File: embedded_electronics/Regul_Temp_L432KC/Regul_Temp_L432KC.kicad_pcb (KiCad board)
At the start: 2 copper layers, 88.9 x 70.1 mm, 31 parts, among them J1 TRIM_CONSIGNE, J11 Digilent Motor, J12 2.54 motor, J2 Temp_In, J3 POWER_IN_5V, J4 SW_MODE, J5 OUT_to_BNC, J6 Consigne, J7 Erreur, J8 OLED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

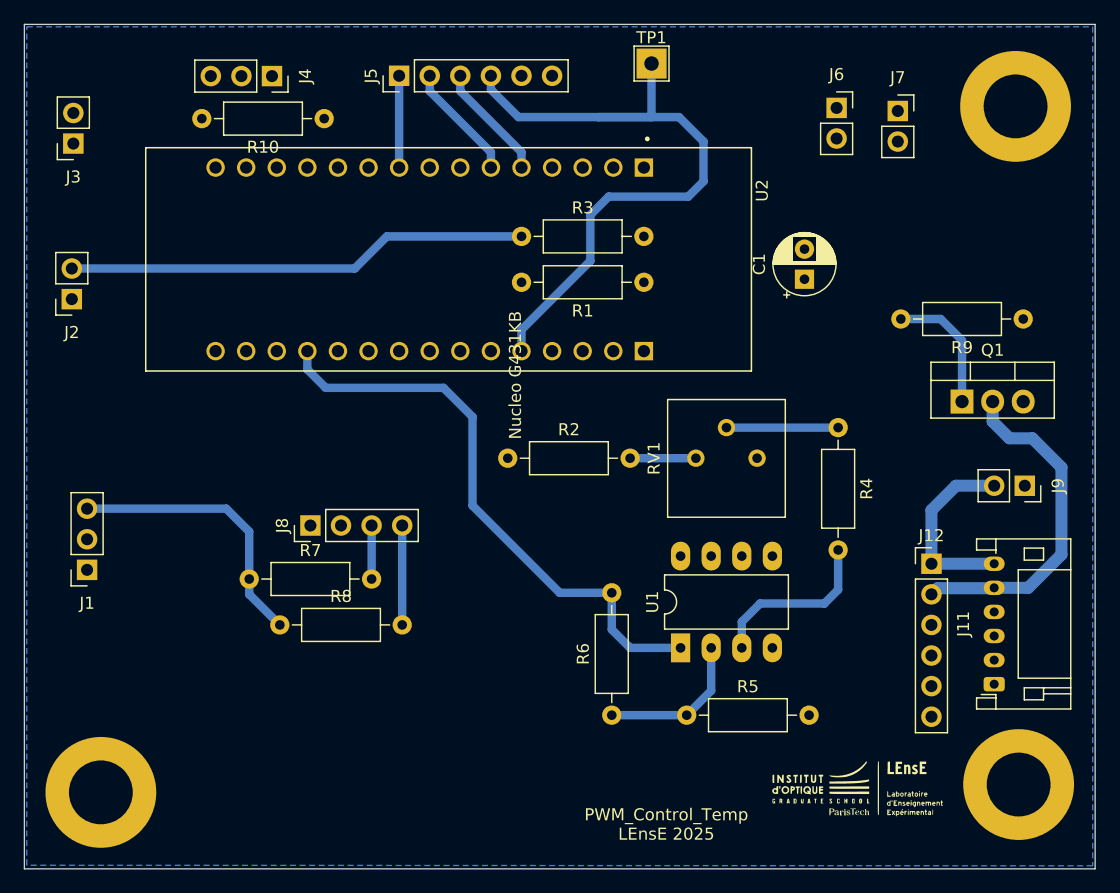
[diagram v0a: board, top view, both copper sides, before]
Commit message: Update PCB of Regulation platform
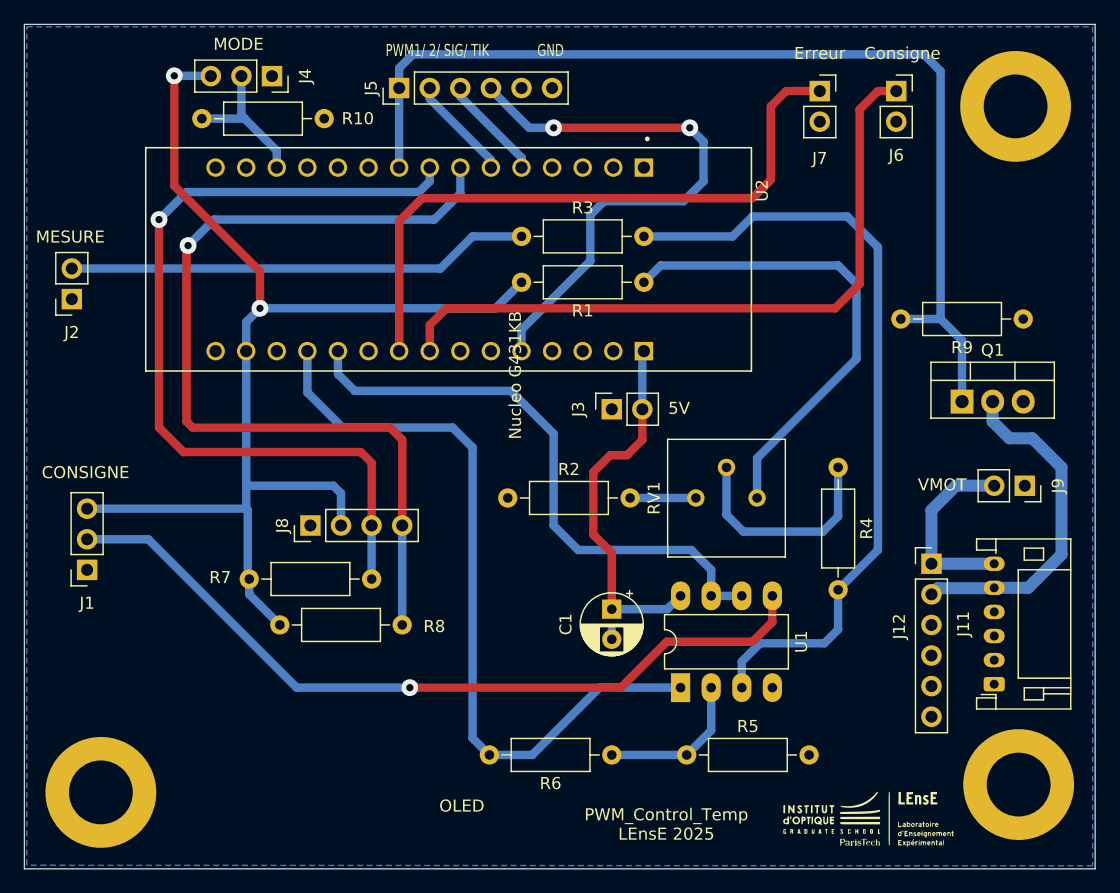
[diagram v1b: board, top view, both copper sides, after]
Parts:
- removed TP1: TestPoint, TestPoint:TestPoint_THTPad_2.5x2.5mm_Drill1.2mm
- moved J3 49.8 mm to (226.6, 116.8), turned to 90 degrees
- moved C1 31.7 mm to (226.6, 133.4), turned to -90 degrees
- moved J7 6.68 mm to (243.8, 90.4)
- moved J6 5.15 mm to (250.2, 90.4)
- moved U1 3.30 mm to (232.3, 140.0)
- moved R2 3.30 mm to (217.9, 124.2)
- moved RV1 3.30 mm to (238.6, 124.2)
- moved R4 3.30 mm to (245.4, 121.7)
- moved R5 3.30 mm to (232.8, 145.5)
- moved R6 3.30 mm to (226.6, 145.5), turned to 180 degrees
- moved G*** 2.68 mm to (247.9, 150.6)
- moved J5 1.02 mm to (208.9, 90.2)
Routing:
- net 3.3V: track 23.1 -> 99.8 mm, vias 0 -> 2
- net PWM1: track 18.5 -> 85.7 mm
- net SDA: track 8.26 -> 75.1 mm, vias 0 -> 1
- net Net-(J1-Pin_2): track 0.00 -> 66.4 mm, vias 0 -> 1
- net SCL: track 4.45 -> 70.7 mm, vias 0 -> 1
- net DAC2_OUT: track 0.00 -> 57.4 mm
- net DAC1_OUT: track 0.00 -> 53.8 mm
- net Net-(U1A-+): track 14.6 -> 65.5 mm
- net T_CONSIGNE: track 0.00 -> 48.8 mm
- net Net-(R1-Pad1): track 0.00 -> 40.1 mm
- net Vin: track 0.00 -> 30.8 mm
- net T_MESURE: track 48.2 -> 63.3 mm
- net CHOICE: track 0.00 -> 12.4 mm
- net TIK: track 57.0 -> 47.0 mm, vias 0 -> 2
- net Net-(R4-Pad1): track 9.27 -> 18.4 mm
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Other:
- board text added: "5V"
- board text added: "CONSIGNE"
- board text added: "Consigne"
- board text added: "Erreur"
- board text added: "GND"
- board text added: "MESURE"
- board text added: "MODE"
- board text added: "OLED"
- board text added: "PWM1/ 2/ SIG/ TIK"
- board text added: "VMOT"

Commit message: Update Regulation temperature
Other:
- board text added: "Mesure"
- board text removed: "Consigne"
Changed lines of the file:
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@@
 		(tags "Through hole socket strip THT 1x02 2.54mm single row")
 		(property "Reference" "J3"
-			(at 0 -2.77 270)
+			(at 0 -2.77 -90)
 			(layer "F.SilkS")
 			(effects
@@
 		)
 		(property "Value" "POWER_IN_5V"
-			(at 0 5.31 270)
+			(at 0 5.31 -90)
 			(layer "F.Fab")
 			(effects
@@
 		)
 		(fp_text user "${REFERENCE}"
-			(at 0 1.27 360)
+			(at 0 1.27 0)
 			(layer "F.Fab")
 			(effects
@@
 		)
 	)
-	(gr_text "Consigne"
+	(gr_text "Mesure"
 		(at 250.698 87.884 0)
 		(layer "F.SilkS")
@@
 	)
 	(gr_text "Nucleo G431KB"
-		(at 219.15 119.35 90)
+		(at 187.863357 115.536355 0)
 		(layer "F.SilkS")
 		(effects

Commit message: Update Regul temp
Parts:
- added J13: Consigne_In, Connector_PinSocket_2.54mm:PinSocket_1x02_P2.54mm_Vertical, F.Cu at (183.1, 128.0)
- added J14: SW_consigne, Connector_PinSocket_2.54mm:PinSocket_1x03_P2.54mm_Vertical, F.Cu at (183.1, 135.8)
- moved J1 7.24 mm to (183.0, 122.9)
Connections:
- J1 pad 2: Net-(J1-Pin_2) -> T_consigne
- U1 pad 5: Net-(J1-Pin_2) -> Net-(J14-Pin_2)
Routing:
- net Net-(J1-Pin_2): track 66.4 -> 0.00 mm, vias 1 -> 0
- net Net-(J14-Pin_2): track 0.00 -> 61.9 mm, vias 0 -> 1
- net T_consigne: track 0.00 -> 25.5 mm
- net In_consigne: track 0.00 -> 5.21 mm
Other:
- board text added: "SWITCH"
- board text added: "TRIM"

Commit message: Update Regul Temp / Debugging LCD screen and test of Follower
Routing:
- net TIK: track 47.0 -> 0.00 mm, vias 2 -> 0
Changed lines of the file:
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@@
-	)
-	(segment
-		(start 221.742 93.472)
-		(end 233.045 93.472)
-		(width 0.7)
-		(layer "F.Cu")
-		(net 6)
-	)
-	(via
-		(at 221.742 93.472)
-		(size 1.4)
-		(drill 0.6)
-		(layers "F.Cu" "B.Cu")
-		(net 6)
-	)
-	(via
-		(at 233.045 93.472)
-		(size 1.4)
-		(drill 0.6)
-		(layers "F.Cu" "B.Cu")
-		(net 6)
-	)
-	(segment
-		(start 224.79 104.521)
-		(end 219.075 110.236)
-		(width 0.7)
-		(layer "B.Cu")
-		(net 6)
-	)
-	(segment
-		(start 225.933 99.568)
-		(end 224.79 100.711)
-		(width 0.7)
-		(layer "B.Cu")
-		(net 6)
-	)
-	(segment
-		(start 234.188 94.615)
-		(end 234.188 97.917)
-		(width 0.7)
-		(layer "B.Cu")
-		(net 6)
-	)
-	(segment
-		(start 232.537 99.568)
-		(end 225.933 99.568)
-		(width 0.7)
-		(layer "B.Cu")
-		(net 6)
-	)
-	(segment
-		(start 216.535 90.297)
-		(end 219.71 93.472)
-		(width 0.7)
-		(layer "B.Cu")
-		(net 6)
-	)
-	(segment
-		(start 233.045 93.472)
-		(end 234.188 94.615)
-		(width 0.7)
-		(layer "B.Cu")
-		(net 6)
-	)
-	(segment
-		(start 234.188 97.917)
-		(end 232.537 99.568)
-		(width 0.7)
-		(layer "B.Cu")
-		(net 6)
-	)
-	(segment
-		(start 224.79 100.711)
-		(end 224.79 104.521)
-		(width 0.7)
-		(layer "B.Cu")
-		(net 6)
-	)
-	(segment
-		(start 219.71 93.472)
-		(end 221.742 93.472)
-		(width 0.7)
-		(layer "B.Cu")
-		(net 6)
-	)
-	(segment
-		(start 219.075 110.236)
-		(end 219.075 112.014)
-		(width 0.7)
-		(layer "B.Cu")
-		(net 6)
 	)
 	(segment
